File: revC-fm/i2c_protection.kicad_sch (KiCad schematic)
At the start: 18 parts, among them Q23 MMDT5551-7-F, Q24 MMDT5551-7-F, Q28 BSS138DWQ-7, Q29 BSS138DWQ-7

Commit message: updated fab files
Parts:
- C71, C72: Manufacturer (none) -> TDK; Mfr. Part No (none) -> CGA2B3X7S2A103K050BB
- Q23, Q24: Manufacturer (none) -> Diodes Incorporated; Mfr. Part No (none) -> MMDT5551-7-F
- Q28, Q29: Manufacturer (none) -> Diodes Incorporated; Mfr. Part No (none) -> BSS138DWQ-7
- R100, R93, R94, R99: Manufacturer (none) -> Stackpole Electronics; Mfr. Part No (none) -> RMCF0402FT10K0
- R103, R104: Manufacturer (none) -> Stackpole Electronics; Mfr. Part No (none) -> RMCF0402FT680R
- R111, R112: Manufacturer (none) -> Stackpole Electronics; Mfr. Part No (none) -> RMCF0402FT100K
- R115, R116: Manufacturer (none) -> Stackpole Electronics; Mfr. Part No (none) -> RMCF0402FT200K
- R138, R141: Manufacturer (none) -> Stackpole Electronics; Mfr. Part No (none) -> RMCF0603ZT0R00

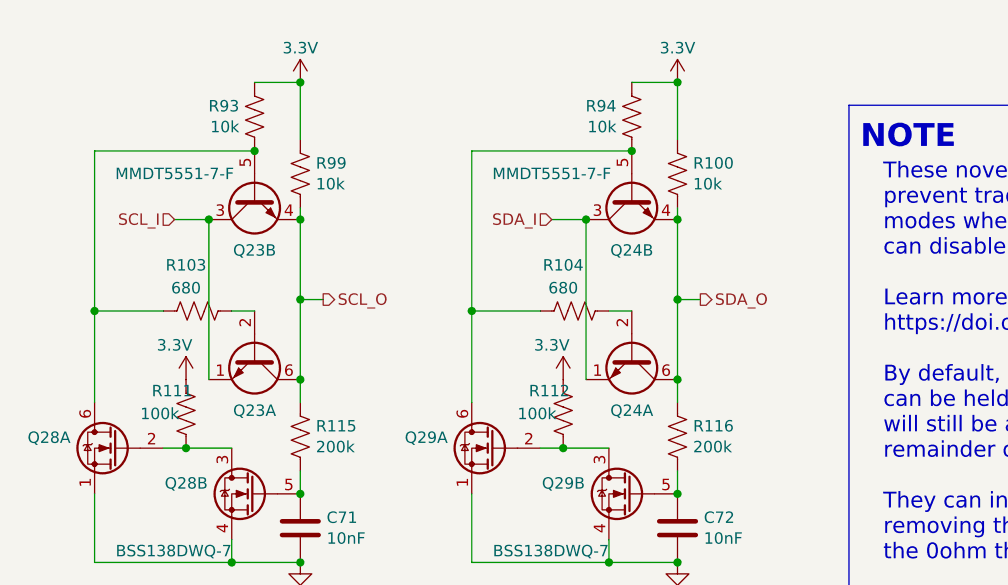
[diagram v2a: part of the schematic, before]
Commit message: updated per review, improved docs
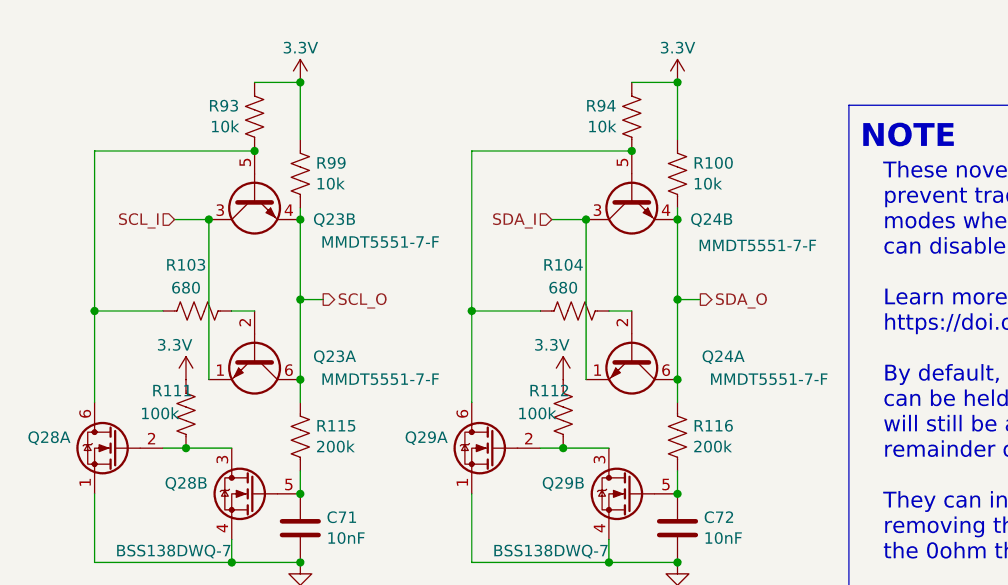
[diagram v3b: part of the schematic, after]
